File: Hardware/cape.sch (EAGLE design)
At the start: 67 parts, among them IC1 RT7258, IC2 RT7258, J1 JST-BM07B-GHS-TBT, J10 JST-BM07B-GHS-TBT, J11 JST-BM07B-GHS-TBT, J12 JST-BM07B-GHS-TBT, J13 JST-BM07B-GHS-TBT, J14 JST-BM07B-GHS-TBT, J15 JST-BM07B-GHS-TBT, J16 JST-BM07B-GHS-TBT, J17 JST-BM07B-GHS-TBT, J18 JST-BM07B-GHS-TBT, J19 JST-BM07B-GHS-TBT, J2 JST-BM07B-GHS-TBT, J20 JST-BM07B-GHS-TBT, J21 JST-BM07B-GHS-TBT, J22 JST-BM07B-GHS-TBT, J23 JST-BM07B-GHS-TBT, J24 JST-BM07B-GHS-TBT, J25 JST-BM07B-GHS-TBT, J26 JST-BM07B-GHS-TBT, J27 JST-BM07B-GHS-TBT, J28 JST-BM07B-GHS-TBT, J29 JST-BM07B-GHS-TBT, J3 JST-BM07B-GHS-TBT, J30 JST-BM07B-GHS-TBT, J31 JST-BM07B-GHS-TBT, J32 JST-BM07B-GHS-TBT, J4 JST-BM07B-GHS-TBT, J5 JST-BM07B-GHS-TBT, J6 JST-BM07B-GHS-TBT, J7 JST-BM07B-GHS-TBT, J8 JST-BM07B-GHS-TBT, J9 JST-BM07B-GHS-TBT, Q1 FDS6670, Q2 FDS6670, X1 RJ45-6L2-B, X2 RJ45-6L2-B

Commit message: added circuits to control backlights, but I'm going to pull them out for this revision
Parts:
- removed U$2: USBA, Livestream:USBA
- added IC3: 74HC125, TotU:74HC125
- added IC4, IC5, IC6, IC7: 74LS595D, SparkFun-DigitalIC:74LS595D
- added Q10, Q11, Q12, Q13, Q14, Q15, Q16, Q17, Q18, Q3, Q4, Q5, Q6, Q7, Q8, Q9: MOSFET-N-DUAL, TotU:MOSFET-N-DUAL
- added R10, R11, R12, R13, R14, R15, R16, R17, R18, R19, R20, R21, R22, R23, R24, R25, R26, R27, R28, R29, R30, R31, R32, R33, R34, R35, R36, R37, R38, R7, R8, R9: 12R/0.5W, SparkFun-Resistors:RESISTOR0805-RES
- added R39: 10k, SparkFun-Passives:RESISTOR1206
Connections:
- removed net LED: J1.6, J10.6, J11.6, J12.6, J13.6, J14.6, J15.6, J16.6, J17.6, J18.6, J19.6, J2.6, J20.6, J21.6, J22.6, J23.6, J24.6, J25.6, J26.6, J27.6, J28.6, J29.6, J3.6, J30.6, J31.6, J32.6, J4.6, J5.6, J6.6, J7.6, J8.6, J9.6
- removed net SDI-2: J2.4
- new net BL_LATCH: IC4.RCK, IC5.RCK, IC6.RCK, IC7.RCK
- new net BL_MOSI: IC4.SER
- new net BL_OE: IC4.G, IC5.G, IC6.G, IC7.G, R39.1
- new net BL_SCK: IC4.SCK, IC5.SCK, IC6.SCK, IC7.SCK
- new net DC_RAW: IC3.2A
- new net LED-1: J1.7, R7.2
- new net LED-10: J10.7, R16.2
- new net LED-11: J11.7, R17.2
- new net LED-12: J12.7, R18.2
- new net LED-13: J13.7, R19.2
- new net LED-14: J14.7, R20.2
- new net LED-15: J15.7, R21.2
- new net LED-16: J16.7, R22.2
- new net LED-17: J17.7, R23.2
- new net LED-18: J18.7, R24.2
- new net LED-19: J19.7, R25.2
- new net LED-2: J2.7, R8.2
- new net LED-20: J20.7, R26.2
- new net LED-21: J21.7, R27.2
- new net LED-22: J22.7, R28.2
- new net LED-23: J23.7, R29.2
- new net LED-24: J24.7, R30.2
- new net LED-25: J25.7, R31.2
- new net LED-26: J26.7, R32.2
- new net LED-27: J27.7, R33.2
- new net LED-28: J28.7, R34.2
- new net LED-29: J29.7, R35.2
- new net LED-3: J3.7, R9.2
- new net LED-30: J30.7, R36.2
- new net LED-31: J31.7, R37.2
- new net LED-32: J32.7, R38.2
- new net LED-4: J4.7, R10.2
- new net LED-5: J5.7, R11.2
- new net LED-6: J6.7, R12.2
- new net LED-7: J7.7, R13.2
- new net LED-8: J8.7, R14.2
- new net LED-9: J9.7, R15.2
- new net N$13: Q4G$2.D, R10.1
- new net N$16: Q3G$1.D, R7.1
- new net N$17: Q3G$2.D, R8.1
- new net N$18: Q5G$1.D, R11.1
- new net N$19: Q5G$2.D, R12.1
- new net N$20: Q6G$1.D, R13.1
- new net N$21: Q6G$2.D, R14.1
- new net N$22: Q7G$1.D, R15.1
- new net N$23: Q7G$2.D, R16.1
- new net N$24: Q8G$1.D, R17.1
- new net N$25: Q8G$2.D, R18.1
- new net N$26: Q9G$1.D, R19.1
- new net N$27: Q9G$2.D, R20.1
- new net N$28: Q10G$1.D, R21.1
- new net N$29: Q10G$2.D, R22.1
- new net N$30: Q11G$1.D, R23.1
- new net N$31: Q11G$2.D, R24.1
- new net N$32: Q12G$1.D, R25.1
- new net N$33: Q12G$2.D, R26.1
- new net N$34: Q13G$1.D, R27.1
- new net N$35: Q13G$2.D, R28.1
- new net N$36: Q14G$1.D, R29.1
- new net N$37: Q14G$2.D, R30.1
- new net N$38: Q15G$1.D, R31.1
- new net N$39: Q15G$2.D, R32.1
- new net N$40: Q16G$1.D, R33.1
- new net N$41: Q16G$2.D, R34.1
- new net N$42: Q17G$1.D, R35.1
- new net N$43: Q17G$2.D, R36.1
- new net N$44: Q18G$1.D, R37.1
- new net N$45: Q18G$2.D, R38.1
- new net N$46: IC4.QH*, IC5.SER
- new net N$47: IC6.QH*, IC7.SER
- new net N$48: IC5.QH*, IC6.SER
- new net N$5: Q4G$1.D, R9.1
- new net N$6: IC3.4A
- new net PWM-1: IC4.QA, Q3G$1.G
- new net PWM-10: IC5.QB, Q7G$2.G
- new net PWM-11: IC5.QC, Q8G$1.G
- new net PWM-12: IC5.QD, Q8G$2.G
- new net PWM-13: IC5.QE, Q9G$1.G
- new net PWM-14: IC5.QF, Q9G$2.G
- new net PWM-15: IC5.QG, Q10G$1.G
- new net PWM-16: IC5.QH, Q10G$2.G
- new net PWM-17: IC6.QA, Q11G$1.G
- new net PWM-18: IC6.QB, Q11G$2.G
- new net PWM-19: IC6.QC, Q12G$1.G
- new net PWM-2: IC4.QB, Q3G$2.G
- new net PWM-20: IC6.QD, Q12G$2.G
- new net PWM-21: IC6.QE, Q13G$1.G
- new net PWM-22: IC6.QF, Q13G$2.G
- new net PWM-23: IC6.QG, Q14G$1.G
- new net PWM-24: IC6.QH, Q14G$2.G
- new net PWM-25: IC7.QA, Q15G$1.G
- new net PWM-26: IC7.QB, Q15G$2.G
- new net PWM-27: IC7.QC, Q16G$1.G
- new net PWM-28: IC7.QD, Q16G$2.G
- new net PWM-29: IC7.QE, Q17G$1.G
- new net PWM-3: IC4.QC, Q4G$1.G
- new net PWM-30: IC7.QF, Q17G$2.G
- new net PWM-31: IC7.QG, Q18G$1.G
- new net PWM-32: IC7.QH, Q18G$2.G
- new net PWM-4: IC4.QD, Q4G$2.G
- new net PWM-5: IC4.QE, Q5G$1.G
- new net PWM-6: IC4.QF, Q5G$2.G
- new net PWM-7: IC4.QG, Q6G$1.G
- new net PWM-8: IC4.QH, Q6G$2.G
- new net PWM-9: IC5.QA, Q7G$1.G
- new net RST_RAW: IC3.3A
- new net SCL_RAW: IC3.1A
- net GND: now also IC3.1OE, IC3.2OE, IC3.3OE, IC3.4OE, IC3.GND, IC4.GND, IC5.GND, IC6.GND, IC7.GND, J1.4, J10.4, J11.4, J12.4, J13.4, J14.4, J15.4, J16.4, J17.4, J18.4, J19.4, J2.4, J20.4, J21.4, J22.4, J23.4, J24.4, J25.4, J26.4, J27.4, J28.4, J29.4, J3.4, J30.4, J31.4, J32.4, J4.4, J5.4, J6.4, J7.4, J8.4, J9.4, Q10G$1.S, Q10G$2.S, Q11G$1.S, Q11G$2.S, Q12G$1.S, Q12G$2.S, Q13G$1.S, Q13G$2.S, Q14G$1.S, Q14G$2.S, Q15G$1.S, Q15G$2.S, Q16G$1.S, Q16G$2.S, Q17G$1.S, Q17G$2.S, Q18G$1.S, Q18G$2.S, Q3G$1.S, Q3G$2.S, Q4G$1.S, Q4G$2.S, Q5G$1.S, Q5G$2.S, Q6G$1.S, Q6G$2.S, Q7G$1.S, Q7G$2.S, Q8G$1.S, Q8G$2.S, Q9G$1.S, Q9G$2.S, U$1.GND@1, U$1.GND@2, U$1.GND@3, U$1.GND@4, U$1.GND@5, U$1.GND@6, U$1.GND@7, U$1.GND@8; no longer J1.1, J10.1, J11.1, J12.1, J13.1, J14.1, J15.1, J16.1, J17.1, J18.1, J19.1, J2.1, J20.1, J21.1, J22.1, J23.1, J24.1, J25.1, J26.1, J27.1, J28.1, J29.1, J3.1, J30.1, J31.1, J32.1, J4.1, J5.1, J6.1, J7.1, J8.1, J9.1, U$2.GND
- net SDI-1: now also J1.1, J2.1; no longer J1.4
- net SDI-10: now also J10.1; no longer J10.4
- net SDI-11: now also J11.1; no longer J11.4
- net SDI-12: now also J12.1; no longer J12.4
- net SDI-13: now also J13.1; no longer J13.4
- net SDI-14: now also J14.1; no longer J14.4
- net SDI-15: now also J15.1; no longer J15.4
- net SDI-16: now also J16.1; no longer J16.4
- net SDI-17: now also J17.1; no longer J17.4
- net SDI-18: now also J18.1; no longer J18.4
- net SDI-19: now also J19.1; no longer J19.4
- net SDI-20: now also J20.1; no longer J20.4
- net SDI-21: now also J21.1; no longer J21.4
- net SDI-22: now also J22.1; no longer J22.4
- net SDI-23: now also J23.1; no longer J23.4
- net SDI-24: now also J24.1; no longer J24.4
- net SDI-25: now also J25.1; no longer J25.4
- net SDI-26: now also J26.1; no longer J26.4
- net SDI-27: now also J27.1; no longer J27.4
- net SDI-28: now also J28.1; no longer J28.4
- net SDI-29: now also J29.1; no longer J29.4
- net SDI-3: now also J3.1; no longer J3.4
- net SDI-30: now also J30.1; no longer J30.4
- net SDI-31: now also J31.1; no longer J31.4
- net SDI-32: now also J32.1; no longer J32.4
- net SDI-4: now also J4.1; no longer J4.4
- net SDI-5: now also J5.1; no longer J5.4
- net SDI-6: now also J6.1; no longer J6.4
- net SDI-7: now also J7.1; no longer J7.4
- net SDI-8: now also J8.1; no longer J8.4
- net SDI-9: now also J9.1; no longer J9.4
- net VCC3V3: now also IC4.SCL, IC4.VCC, IC5.SCL, IC5.VCC, IC6.SCL, IC6.VCC, IC7.SCL, IC7.VCC, J1.6, J10.6, J11.6, J12.6, J13.6, J14.6, J15.6, J16.6, J17.6, J18.6, J19.6, J2.6, J20.6, J21.6, J22.6, J23.6, J24.6, J25.6, J26.6, J27.6, J28.6, J29.6, J3.6, J30.6, J31.6, J32.6, J4.6, J5.6, J6.6, J7.6, J8.6, J9.6, R39.2; no longer J1.7, J10.7, J11.7, J12.7, J13.7, J14.7, J15.7, J16.7, J17.7, J18.7, J19.7, J2.7, J20.7, J21.7, J22.7, J23.7, J24.7, J25.7, J26.7, J27.7, J28.7, J29.7, J3.7, J30.7, J31.7, J32.7, J4.7, J5.7, J6.7, J7.7, J8.7, J9.7
- net VCC5V: now also U$1.VDD_5V@1; no longer U$2.VBUS
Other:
- note added: "24v -> 5v Step Down"
- note added: "5v -> 3.3v Step Down"
- moved on the sheet: C1, C10, C11, C12, C13, C14, C15, C16, C17, C18, C2, C3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

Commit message: removed led drivers, added backlight resistors
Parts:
- removed IC4, IC5, IC6, IC7: 74LS595D, SparkFun-DigitalIC:74LS595D
- removed Q10, Q11, Q12, Q13, Q14, Q15, Q16, Q17, Q18, Q3, Q4, Q5, Q6, Q7, Q8, Q9: MOSFET-N-DUAL, TotU:MOSFET-N-DUAL
- removed R39: 10k, SparkFun-Passives:RESISTOR1206
- R10, R11, R12, R13, R14, R15, R16, R17, R18, R19, R20, R21, R22, R23, R24, R25, R26, R27, R28, R29, R30, R31, R32, R33, R34, R35, R36, R37, R38, R7, R8, R9: value 12R/0.5W -> (none); device SparkFun-Resistors:RESISTOR0805-RES -> SparkFun-Passives:RESISTOR0805-RES
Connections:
- removed net BL_LATCH: IC4.RCK, IC5.RCK, IC6.RCK, IC7.RCK
- removed net BL_MOSI: IC4.SER
- removed net BL_OE: IC4.G, IC5.G, IC6.G, IC7.G, R39.1
- removed net BL_SCK: IC4.SCK, IC5.SCK, IC6.SCK, IC7.SCK
- removed net N$13: Q4G$2.D, R10.1
- removed net N$16: Q3G$1.D, R7.1
- removed net N$17: Q3G$2.D, R8.1
- removed net N$18: Q5G$1.D, R11.1
- removed net N$19: Q5G$2.D, R12.1
- removed net N$20: Q6G$1.D, R13.1
- removed net N$21: Q6G$2.D, R14.1
- removed net N$22: Q7G$1.D, R15.1
- removed net N$23: Q7G$2.D, R16.1
- removed net N$24: Q8G$1.D, R17.1
- removed net N$25: Q8G$2.D, R18.1
- removed net N$26: Q9G$1.D, R19.1
- removed net N$27: Q9G$2.D, R20.1
- removed net N$28: Q10G$1.D, R21.1
- removed net N$29: Q10G$2.D, R22.1
- removed net N$30: Q11G$1.D, R23.1
- removed net N$31: Q11G$2.D, R24.1
- removed net N$32: Q12G$1.D, R25.1
- removed net N$33: Q12G$2.D, R26.1
- removed net N$34: Q13G$1.D, R27.1
- removed net N$35: Q13G$2.D, R28.1
- removed net N$36: Q14G$1.D, R29.1
- removed net N$37: Q14G$2.D, R30.1
- removed net N$38: Q15G$1.D, R31.1
- removed net N$39: Q15G$2.D, R32.1
- removed net N$40: Q16G$1.D, R33.1
- removed net N$41: Q16G$2.D, R34.1
- removed net N$42: Q17G$1.D, R35.1
- removed net N$43: Q17G$2.D, R36.1
- removed net N$44: Q18G$1.D, R37.1
- removed net N$45: Q18G$2.D, R38.1
- removed net N$46: IC4.QH*, IC5.SER
- removed net N$47: IC6.QH*, IC7.SER
- removed net N$48: IC5.QH*, IC6.SER
- removed net N$5: Q4G$1.D, R9.1
- removed net PWM-1: IC4.QA, Q3G$1.G
- removed net PWM-10: IC5.QB, Q7G$2.G
- removed net PWM-11: IC5.QC, Q8G$1.G
- removed net PWM-12: IC5.QD, Q8G$2.G
- removed net PWM-13: IC5.QE, Q9G$1.G
- removed net PWM-14: IC5.QF, Q9G$2.G
- removed net PWM-15: IC5.QG, Q10G$1.G
- removed net PWM-16: IC5.QH, Q10G$2.G
- removed net PWM-17: IC6.QA, Q11G$1.G
- removed net PWM-18: IC6.QB, Q11G$2.G
- removed net PWM-19: IC6.QC, Q12G$1.G
- removed net PWM-2: IC4.QB, Q3G$2.G
- removed net PWM-20: IC6.QD, Q12G$2.G
- removed net PWM-21: IC6.QE, Q13G$1.G
- removed net PWM-22: IC6.QF, Q13G$2.G
- removed net PWM-23: IC6.QG, Q14G$1.G
- removed net PWM-24: IC6.QH, Q14G$2.G
- removed net PWM-25: IC7.QA, Q15G$1.G
- removed net PWM-26: IC7.QB, Q15G$2.G
- removed net PWM-27: IC7.QC, Q16G$1.G
- removed net PWM-28: IC7.QD, Q16G$2.G
- removed net PWM-29: IC7.QE, Q17G$1.G
- removed net PWM-3: IC4.QC, Q4G$1.G
- removed net PWM-30: IC7.QF, Q17G$2.G
- removed net PWM-31: IC7.QG, Q18G$1.G
- removed net PWM-32: IC7.QH, Q18G$2.G
- removed net PWM-4: IC4.QD, Q4G$2.G
- removed net PWM-5: IC4.QE, Q5G$1.G
- removed net PWM-6: IC4.QF, Q5G$2.G
- removed net PWM-7: IC4.QG, Q6G$1.G
- removed net PWM-8: IC4.QH, Q6G$2.G
- removed net PWM-9: IC5.QA, Q7G$1.G
- net GND: no longer IC4.GND, IC5.GND, IC6.GND, IC7.GND, Q10G$1.S, Q10G$2.S, Q11G$1.S, Q11G$2.S, Q12G$1.S, Q12G$2.S, Q13G$1.S, Q13G$2.S, Q14G$1.S, Q14G$2.S, Q15G$1.S, Q15G$2.S, Q16G$1.S, Q16G$2.S, Q17G$1.S, Q17G$2.S, Q18G$1.S, Q18G$2.S, Q3G$1.S, Q3G$2.S, Q4G$1.S, Q4G$2.S, Q5G$1.S, Q5G$2.S, Q6G$1.S, Q6G$2.S, Q7G$1.S, Q7G$2.S, Q8G$1.S, Q8G$2.S, Q9G$1.S, Q9G$2.S
- net LED-1: now also R7.1; no longer R7.2
- net LED-10: now also R12.1; no longer R16.2
- net LED-11: now also R13.1; no longer R17.2
- net LED-12: now also R14.1; no longer R18.2
- net LED-13: now also R19.1; no longer R19.2
- net LED-14: now also R20.1; no longer R20.2
- net LED-15: now also R21.1; no longer R21.2
- net LED-16: now also R22.1; no longer R22.2
- net LED-17: now also R23.1; no longer R23.2
- net LED-18: now also R24.1; no longer R24.2
- net LED-19: now also R25.1; no longer R25.2
- net LED-2: now also R8.1; no longer R8.2
- net LED-20: now also R26.1; no longer R26.2
- net LED-21: now also R31.1; no longer R27.2
- net LED-22: now also R32.1; no longer R28.2
- net LED-23: now also R33.1; no longer R29.2
- net LED-24: now also R34.1; no longer R30.2
- net LED-25: now also R27.1; no longer R31.2
- net LED-26: now also R28.1; no longer R32.2
- net LED-27: now also R29.1; no longer R33.2
- net LED-28: now also R30.1; no longer R34.2
- net LED-29: now also R35.1; no longer R35.2
- net LED-3: now also R9.1; no longer R9.2
- net LED-30: now also R36.1; no longer R36.2
- net LED-31: now also R37.1; no longer R37.2
- net LED-32: now also R38.1; no longer R38.2
- net LED-4: now also R10.1; no longer R10.2
- net LED-5: now also R15.1; no longer R11.2
- net LED-6: now also R16.1; no longer R12.2
- net LED-7: now also R17.1; no longer R13.2
- net LED-8: now also R18.1; no longer R14.2
- net LED-9: now also R11.1; no longer R15.2
- net VCC3V3: no longer IC4.SCL, IC4.VCC, IC5.SCL, IC5.VCC, IC6.SCL, IC6.VCC, IC7.SCL, IC7.VCC, R39.2
- net VCC5V: now also R10.2, R11.2, R12.2, R13.2, R14.2, R15.2, R16.2, R17.2, R18.2, R19.2, R20.2, R21.2, R22.2, R23.2, R24.2, R25.2, R26.2, R27.2, R28.2, R29.2, R30.2, R31.2, R32.2, R33.2, R34.2, R35.2, R36.2, R37.2, R38.2, R7.2, R8.2, R9.2
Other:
- moved on the sheet: C1, C10, C11, C12, C13, C14, C15, C16, C17, C18, C2, C3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

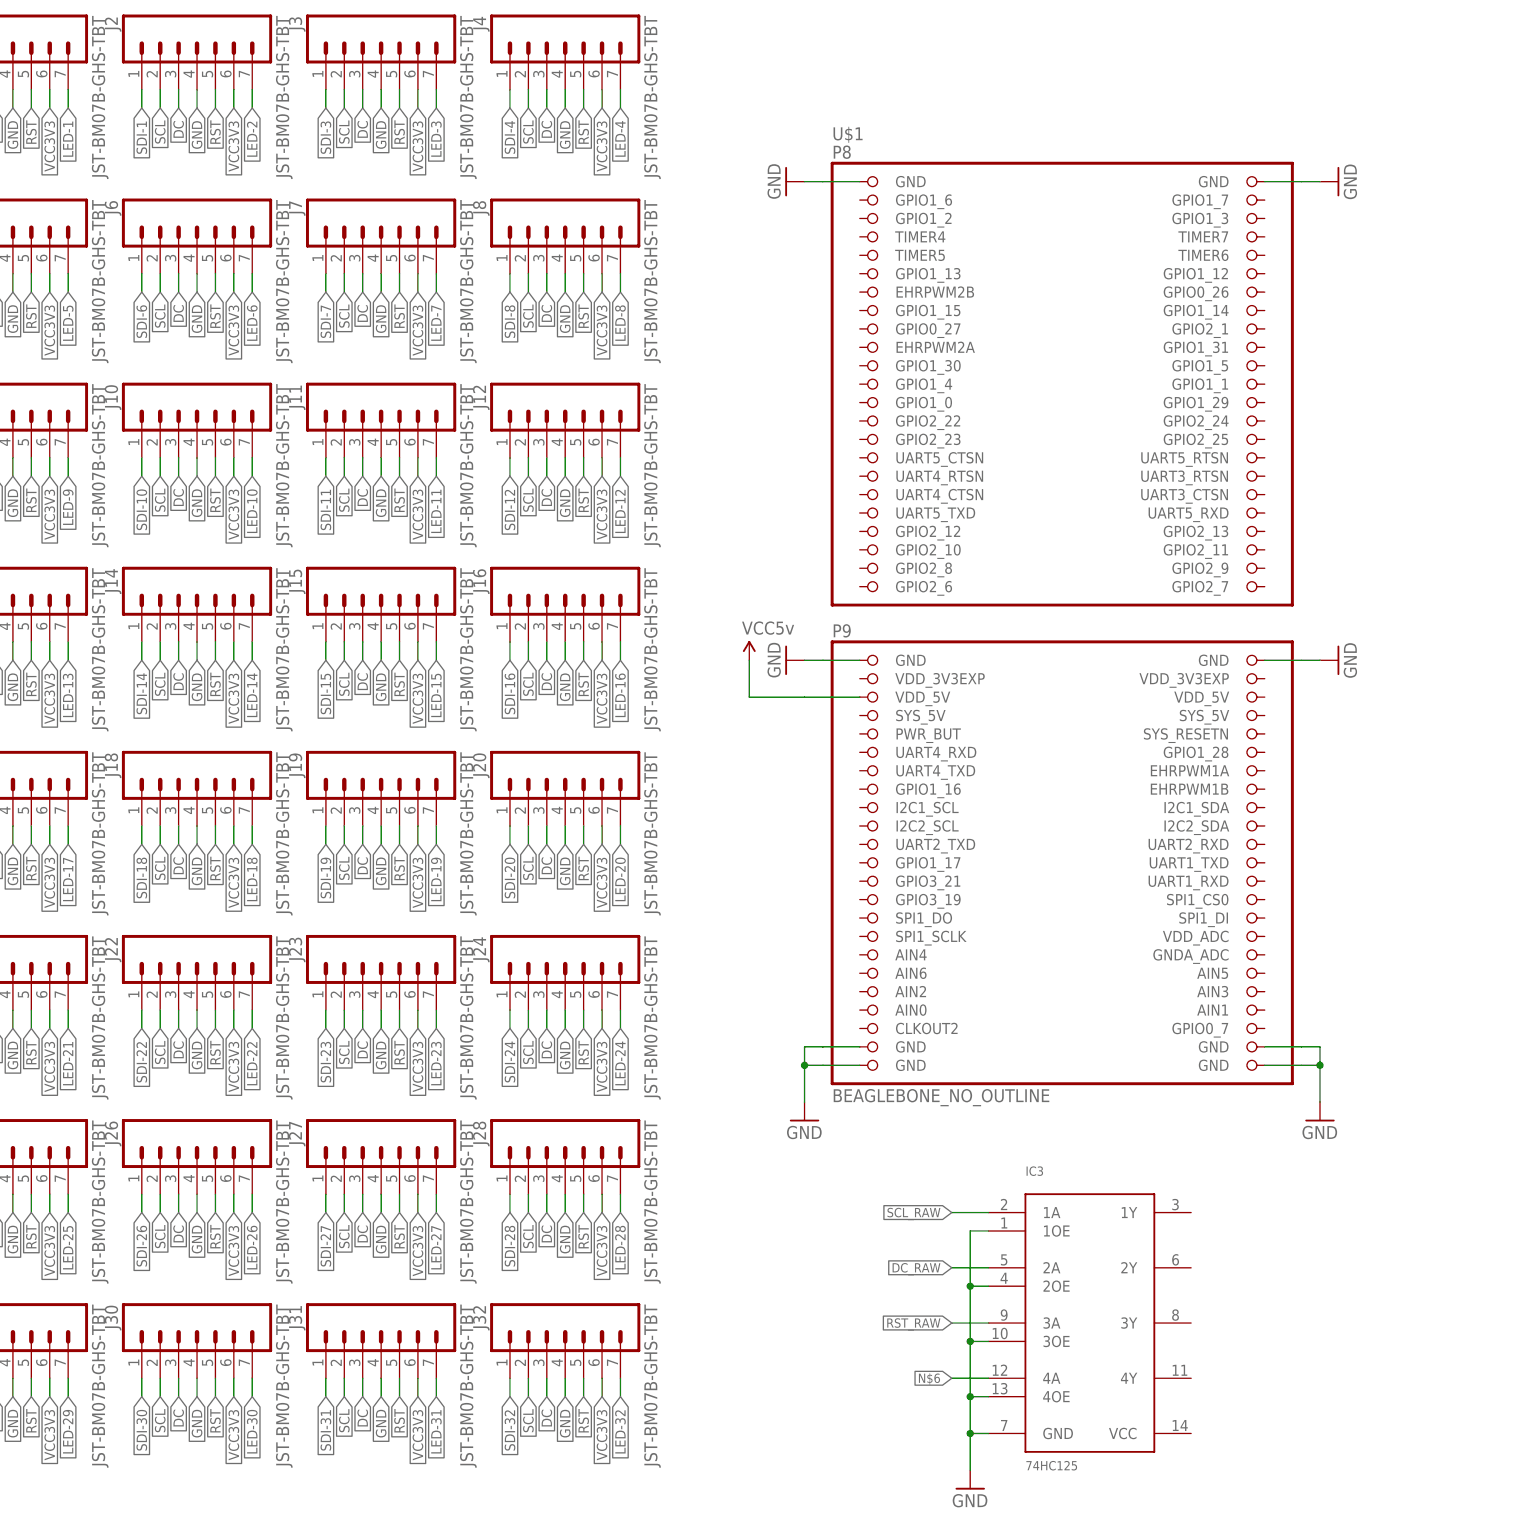
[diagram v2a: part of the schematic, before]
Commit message: routing and pinmapping
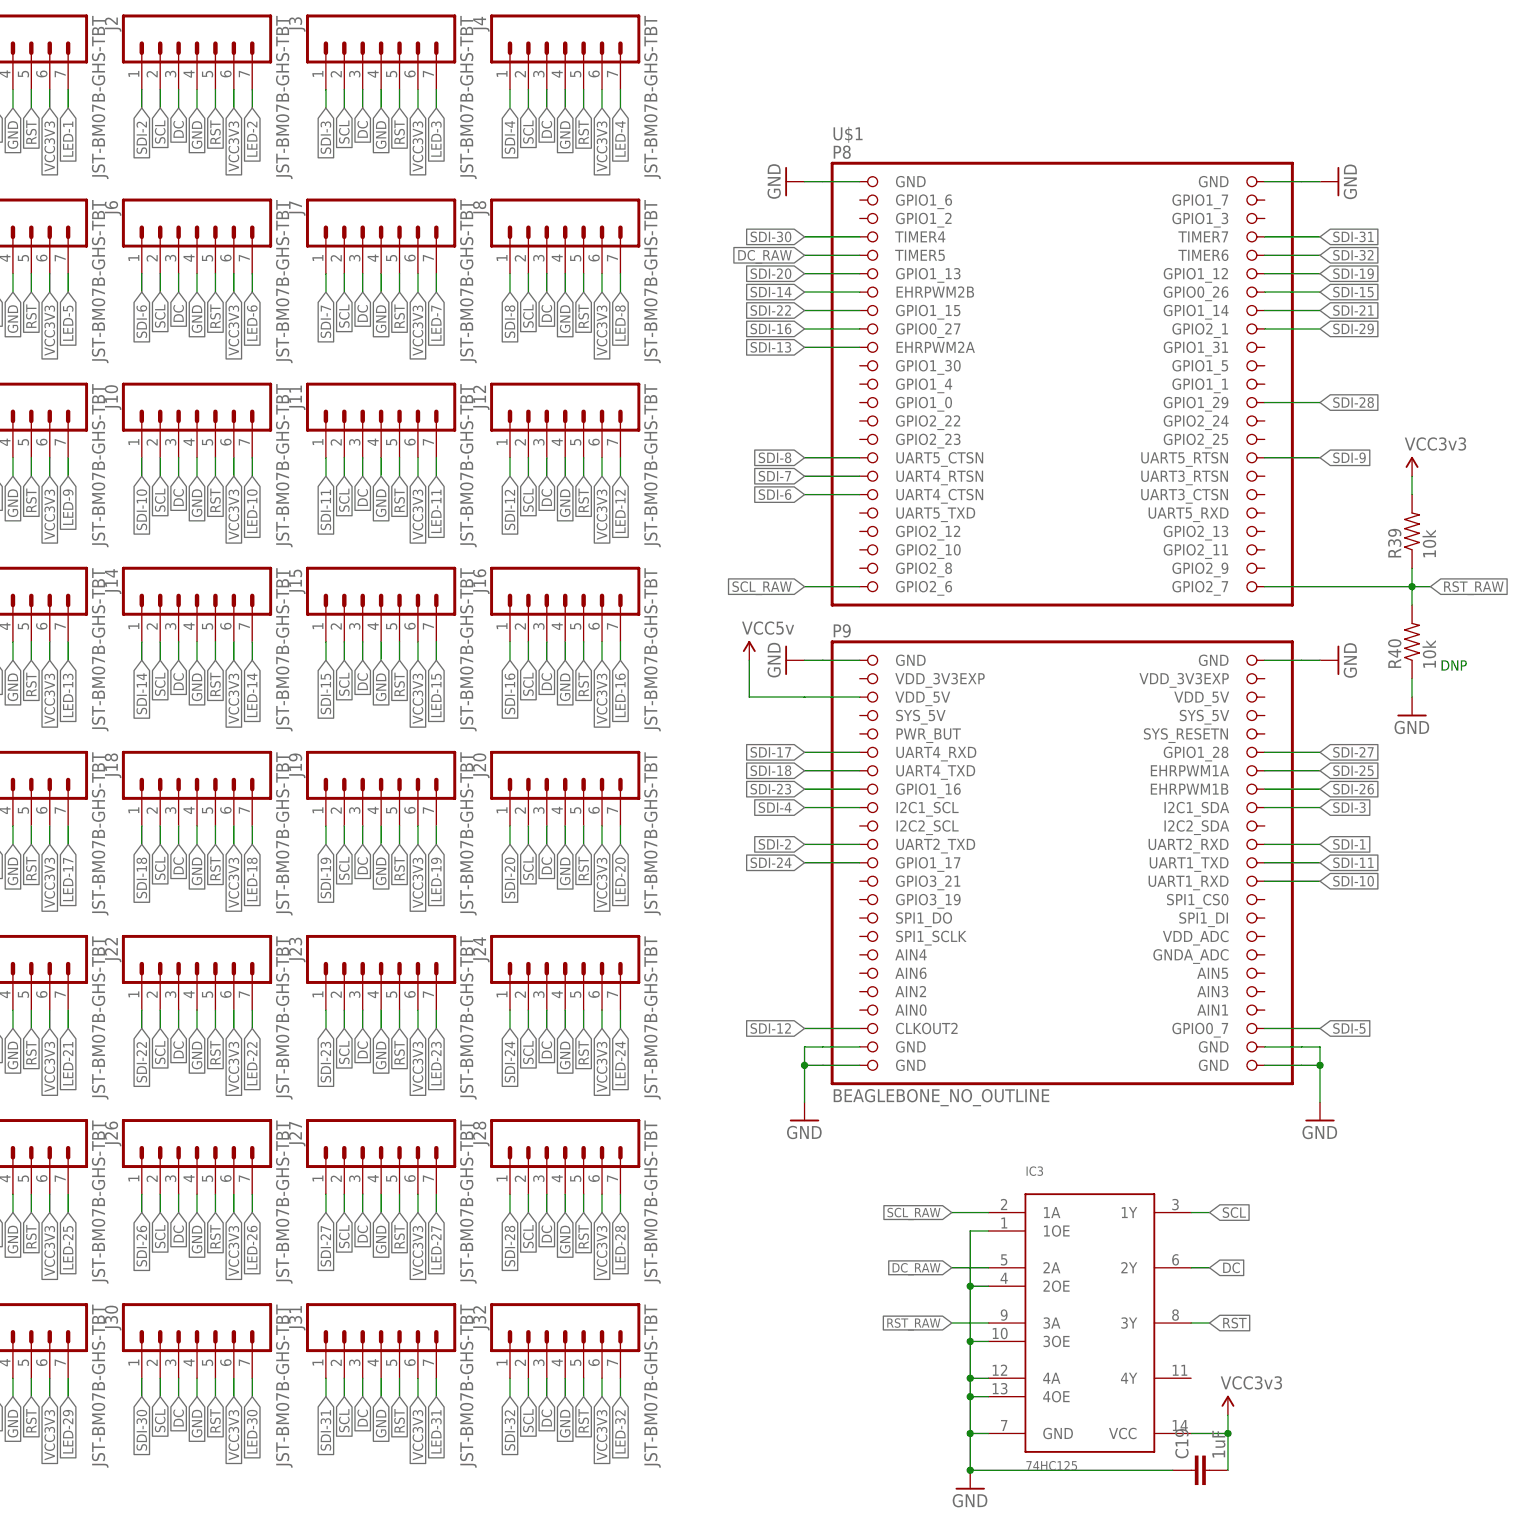
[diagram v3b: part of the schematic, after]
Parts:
- added C19: 1uF, SparkFun-Capacitors:CAP1206
- added R39, R40: 10k, SparkFun-Passives:RESISTOR1206
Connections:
- removed net N$6: IC3.4A
- new net SDI-2: J2.1, U$1.UART2_TXD
- net DC: now also IC3.2Y
- net DC_RAW: now also U$1.TIMER5
- net GND: now also C19.1, IC3.4A, R40.1
- net RST: now also IC3.3Y
- net RST_RAW: now also R39.1, R40.2, U$1.GPIO2_7
- net SCL: now also IC3.1Y
- net SCL_RAW: now also U$1.GPIO2_6
- net SDI-1: now also U$1.UART2_RXD; no longer J2.1
- net SDI-10: now also U$1.UART1_RXD
- net SDI-11: now also U$1.UART1_TXD
- net SDI-12: now also U$1.CLKOUT2
- net SDI-13: now also U$1.EHRPWM2A
- net SDI-14: now also U$1.EHRPWM2B
- net SDI-15: now also U$1.GPIO0_26
- net SDI-16: now also U$1.GPIO0_27
- net SDI-17: now also U$1.UART4_RXD
- net SDI-18: now also U$1.UART4_TXD
- net SDI-19: now also U$1.GPIO1_12
- net SDI-20: now also U$1.GPIO1_13
- net SDI-21: now also U$1.GPIO1_14
- net SDI-22: now also U$1.GPIO1_15
- net SDI-23: now also U$1.GPIO1_16
- net SDI-24: now also U$1.GPIO1_17
- net SDI-25: now also U$1.EHRPWM1A
- net SDI-26: now also U$1.EHRPWM1B
- net SDI-27: now also U$1.GPIO1_28
- net SDI-28: now also U$1.GPIO1_29
- net SDI-29: now also U$1.GPIO2_1
- net SDI-3: now also U$1.I2C1_SDA
- net SDI-30: now also U$1.TIMER4
- net SDI-31: now also U$1.TIMER7
- net SDI-32: now also U$1.TIMER6
- net SDI-4: now also U$1.I2C1_SCL
- net SDI-5: now also U$1.GPIO0_7
- net SDI-6: now also U$1.UART4_CTSN
- net SDI-7: now also U$1.UART4_RTSN
- net SDI-8: now also U$1.UART5_CTSN
- net SDI-9: now also U$1.UART5_RTSN
- net VCC3V3: now also C19.2, IC3.VCC, R39.2
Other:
- note added: "DNP"
